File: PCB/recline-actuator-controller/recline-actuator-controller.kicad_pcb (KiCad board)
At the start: 4 copper layers, 140 x 100 mm, 171 parts, among them J1 DX07S016JA1R1500, J10 1757242, J11 1757242, J12 0705430002, J13 0705430002, J14 0705430002, J15 0705430002, J16 1757242, J17 1757242, J18 0705430002, J19 0705430002, J2 Conn_01x03, J20 0705430002, J21 0705430002, J22 1757242, J3 RJHSE-5381, J4 1757242, J5 1757242, J6 1757242, J7 1757242, J8 1757242, J9 1757242, M1 D24V22F5, M2 D24V22F3, Q1 PSMN7R0-60YS,115, Q2 PSMN7R0-60YS,115, Q3 PSMN7R0-60YS,115, Q4 PSMN7R0-60YS,115, Q5 PSMN7R0-60YS,115, Q6 BSC014N04LSIATMA1, Q7 BSC014N04LSIATMA1, Q8 BSC014N04LSIATMA1, Q9 BSC014N04LSIATMA1, SW1 TL3330AF260QG, SW2 TL3330AF260QG, U1 TEMPLATE, U2 RP2040, U3 MAX3535ECWI+T, U4 VNH5019ATR-E, U5 VNH5019ATR-E, U6 VNH5019ATR-E, U7 VNH5019ATR-E, U8 MCP23S17T-E/ML, X1 ABM8G-12.000MHZ-18-D2Y-T

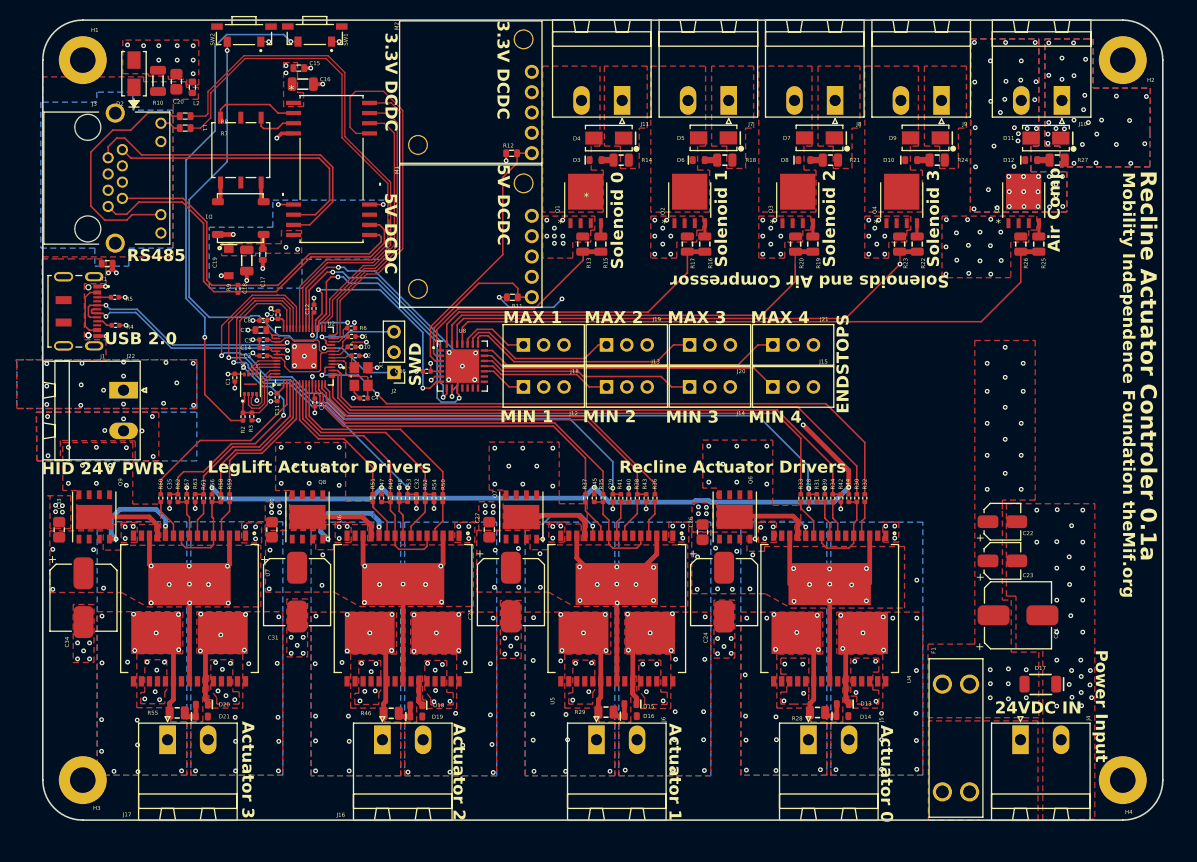
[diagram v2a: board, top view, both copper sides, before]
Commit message: RS485
RS485 schematic corrected, 5V regulator removed.
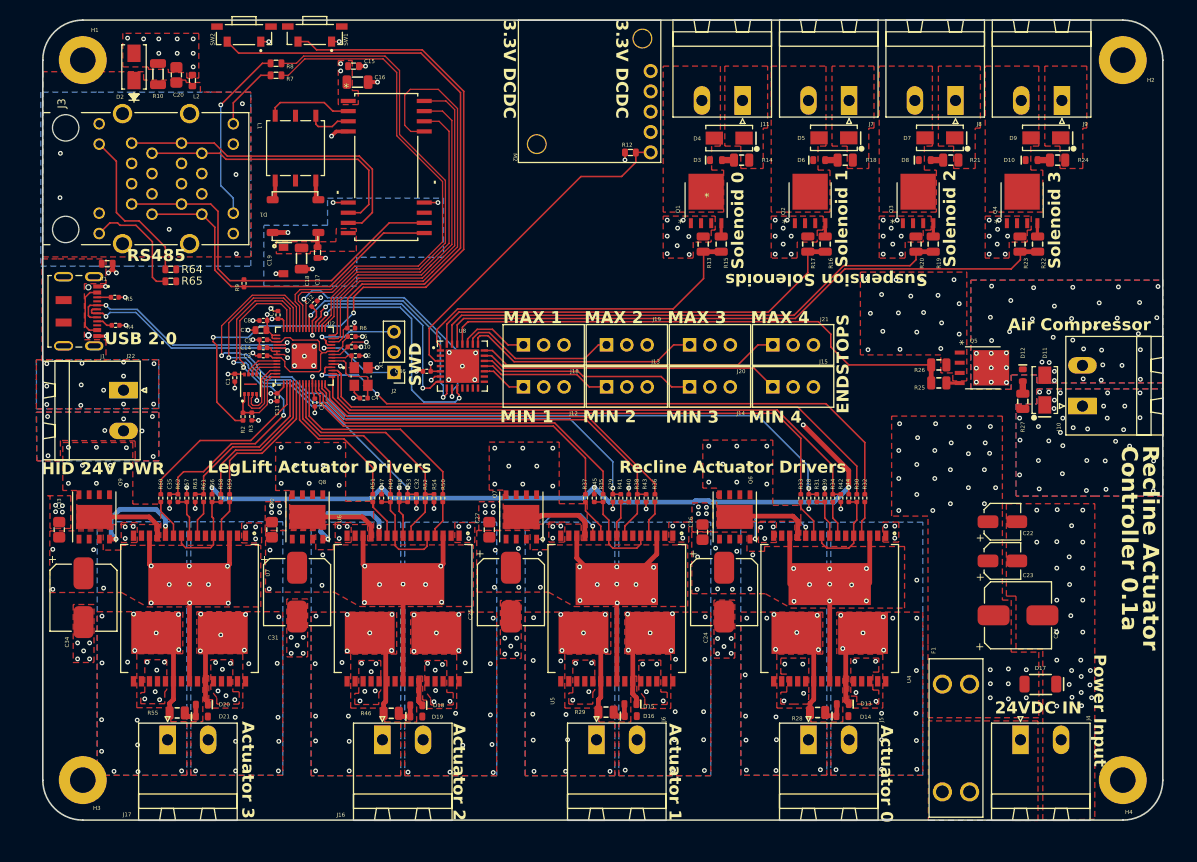
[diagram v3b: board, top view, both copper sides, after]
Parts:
- removed M1: D24V22F5, AVR-KiCAD-Lib-Modules:D24V22F12
- removed R11: RC0603FR-072K2L, AVR-KiCAD-Lib-Resistors:R0603
- added R64: RC0603FR-07470RL, AVR-KiCAD-Lib-Resistors:R0603, F.Cu at (66.0, 76.2)
- added R65: RC0603FR-07470RL, AVR-KiCAD-Lib-Resistors:R0603, F.Cu at (66.0, 77.7)
- J3: value RJHSE-5381 -> RJSAE-538A-02; footprint AVR-KiCAD-Lib-Connectors:AMPHENOL_RJHSE-5381 -> AVR-KiCAD-Lib-Connectors:AMPHENOL_RJSAE538A02
- moved J10 38.3 mm to (180.0, 93.2), turned to 90 degrees
- moved D11 31.5 mm to (175.2, 91.2), turned to 90 degrees
- moved R27 30.5 mm to (172.5, 92.7), turned to -90 degrees
- moved D12 26.9 mm to (172.5, 89.4), turned to 90 degrees
- moved Q5 21.6 mm to (167.5, 88.5), turned to -90 degrees
- moved R25 21.4 mm to (162.0, 90.3), turned to 0 degrees
- moved R26 18.3 mm to (162.0, 88.1), turned to 0 degrees
- moved D3 15.1 mm to (134.2, 62.5)
- moved D4 15.1 mm to (135.8, 59.8)
- moved D6 15.1 mm to (147.1, 62.5)
- moved D8 15.1 mm to (160.2, 62.5)
- moved J8 15.1 mm to (164.1, 55.0)
- moved R13 15.1 mm to (132.6, 73.0)
- moved R15 15.1 mm to (134.8, 73.0)
- moved R16 15.1 mm to (147.8, 73.0)
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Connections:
- net +5V renamed Net-(U3-VCC2)
- J3 pad 3: unconnected-(J3-Pad3) -> GND
- J3 pad 4: unconnected-(J3-Pad4) -> GND
- J3 pad 5: unconnected-(J3-Pad5) -> GND
- J3 pad 6: unconnected-(J3-Pad6) -> GND
- U8 pad 2: /Power/5V_PG -> /End Stop Limit Switches/5V_PG
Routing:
- net Net-(R2-Pad1): track 63.5 -> 92.6 mm
- net Net-(J3-Pad23): track 0.00 -> 20.1 mm
- net /Power/5V_PG: track 20.1 -> 0.00 mm
- net /End Stop Limit Switches/SOLENOID_0: track 28.0 -> 44.4 mm
- net /End Stop Limit Switches/SOLENOID_1: track 40.1 -> 55.1 mm
- net /End Stop Limit Switches/SOLENOID_3: track 64.7 -> 79.4 mm, vias 1 -> 0
- net Net-(J3-Pad21): track 0.00 -> 14.4 mm
- net /End Stop Limit Switches/AIR_COMP: track 80.4 -> 66.5 mm
- net /End Stop Limit Switches/SOLENOID_2: track 53.5 -> 66.9 mm
- net Net-(U2-RUN): track 61.8 -> 74.8 mm, vias 2 -> 0
- net /Power/3.3V_PG: track 33.2 -> 42.6 mm
- net +3.3V: track 137.3 -> 128.6 mm, vias 21 -> 19
- net Net-(J3-Pad10): track 29.8 -> 22.6 mm, vias 0 -> 1
- net /RP2040/RS485_TX_EN: track 34.2 -> 41.4 mm
- net /RP2040/RS485_TXD: track 47.9 -> 54.8 mm
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- removed copper zone on In2.Cu, net Net-(U3-VCC2)
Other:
- board text added: "Air Compressor"
- board text added: "Controller 0.1a"
- board text added: "M3OUTA"
- board text added: "M3OUTB"
- board text added: "M4OUTA"
- board text added: "M4OUTB"
- board text added: "Recline Actuator"
- board text added: "Suspension Solenoids"
- board text removed: "3V3"
- board text removed: "5V DCDC"
- board text removed: "5V PG"
- board text removed: "5V Rail"
- board text removed: "Air Comp"
- board text removed: "MAX1"
- board text removed: "MAX2"
- board text removed: "MIN1"
- board text removed: "MIN2"
- board text removed: "Mobility Independence Foundation theMif.org"
- board text removed: "Recline Actuator Controler 0.1a"
- board text removed: "Solenoids and Air Compressor"

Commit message: RS485
RS485 circuit fixed and PCB topology updated.
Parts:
- moved R1 1.63 mm to (59.2, 76.6)
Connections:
- C20 pad 2: GND -> Earth
- D2 pad 2: GND -> Earth
- J3 pad 15: GND -> Earth
- J3 pad 16: GND -> Earth
- J3 pad 17: GND -> Earth
- J3 pad 18: GND -> Earth
- J3 pad 24: (no net) -> GND
- J3 pad 3: GND -> Earth
- J3 pad 4: GND -> Earth
- J3 pad 5: GND -> Earth
- J3 pad 6: GND -> Earth
- L2 pad 2: GND -> Earth
- R10 pad 1: GND -> Earth
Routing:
- net GND: track 41.9 -> 75.7 mm, vias 221 -> 211
- net Net-(J1-SHIELD-PadS1): vias 0 -> 13
- net Earth: vias 6 -> 42
- added copper zone on F.Cu, net Earth
- added copper zone on In1.Cu, net Earth
- added copper zone on In2.Cu, net Earth
- added copper zone on B.Cu, net Net-(J1-SHIELD-PadS1)
